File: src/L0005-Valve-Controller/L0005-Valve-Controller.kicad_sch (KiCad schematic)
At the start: 16 parts, among them J1 Jumper_NO, P1 3220-20-0200-00

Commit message: routed rev 2
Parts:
- B1: footprint (none) -> L0005-Valve-Controller:PTS647SM38SMTR2LFS
- C15: value (none) -> 0.1uF; footprint (none) -> L0005-Valve-Controller:CAP_0603
- R26, R27: footprint (none) -> L0005-Valve-Controller:RES_0603
- U1: value (none) -> STM32H750VBTx; footprint (none) -> L0005-Valve-Controller:STM32H750VBT6
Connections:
- net EXECPT: now also U1.60 (PD13); no longer U1.78 (PC10)
- net RX: now also U1.79 (PC11); no longer U1.68 (PA9)
- net TX: now also U1.78 (PC10); no longer U1.69 (PA10)
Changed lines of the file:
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@@
   (junction (at 44.45 68.58) (diameter 0) (color 0 0 0 0)
   )
+  (no_connect (at 104.775 124.46))
+  (no_connect (at 47.625 118.11))
+  (no_connect (at 47.625 115.57))
   (no_connect (at 163.83 87.63))
   (no_connect (at 163.83 95.25))
@@
   (no_connect (at 47.625 86.36))
   (no_connect (at 104.775 167.64))
-  (no_connect (at 104.775 165.1))
   (no_connect (at 104.775 149.86))
   (no_connect (at 104.775 147.32))
@@
   (no_connect (at 47.625 162.56))
   (no_connect (at 47.625 165.1))
-  (no_connect (at 47.625 170.18))
   (no_connect (at 47.625 172.72))
   (no_connect (at 104.775 175.26))
@@
   (no_connect (at 104.775 132.08))
   (no_connect (at 104.775 129.54))
-  (no_connect (at 104.775 124.46))
   (no_connect (at 210.82 76.962))
   (no_connect (at 210.82 61.722))
@@
     (stroke (width 0) (type default) (color 0 0 0 0))
   )
+  (wire (pts (xy 36.83 170.18) (xy 47.625 170.18))
+    (stroke (width 0) (type default) (color 0 0 0 0))
+  )
   (wire (pts (xy 104.775 152.4) (xy 113.03 152.4))
     (stroke (width 0) (type default) (color 0 0 0 0))
@@
     (stroke (width 0) (type default) (color 0 0 0 0))
   )
-  (wire (pts (xy 38.735 118.11) (xy 47.625 118.11))
-    (stroke (width 0) (type default) (color 0 0 0 0))
-  )
   (wire (pts (xy 210.82 64.262) (xy 208.28 64.262))
     (stroke (width 0) (type default) (color 0 0 0 0))
@@
     (stroke (width 0) (type default) (color 0 0 0 0))
   )
+  (wire (pts (xy 104.775 165.1) (xy 113.03 165.1))
+    (stroke (width 0) (type default) (color 0 0 0 0))
+  )
   (polyline (pts (xy 174.625 108.585) (xy 133.985 108.585))
     (stroke (width 0) (type default) (color 0 0 0 0))
@@
     (stroke (width 0) (type default) (color 0 0 0 0))
   )
+  (wire (pts (xy 104.775 162.56) (xy 113.03 162.56))
+    (stroke (width 0) (type default) (color 0 0 0 0))
+  )
   (wire (pts (xy 44.45 55.88) (xy 44.45 53.34))
     (stroke (width 0) (type default) (color 0 0 0 0))
@@
     (stroke (width 0) (type default) (color 0 0 0 0))
   )
-  (wire (pts (xy 104.775 162.56) (xy 113.03 162.56))
-    (stroke (width 0) (type default) (color 0 0 0 0))
-  )
   (wire (pts (xy 208.28 74.422) (xy 208.28 79.502))
     (stroke (width 0) (type default) (color 0 0 0 0))
@@
   )
   (wire (pts (xy 104.775 127) (xy 113.03 127))
-    (stroke (width 0) (type default) (color 0 0 0 0))
-  )
-  (wire (pts (xy 47.625 115.57) (xy 38.735 115.57))
     (stroke (width 0) (type default) (color 0 0 0 0))
   )
@@
     )
   )
-  (global_label "RX" (shape input) (at 38.735 115.57 180) (fields_autoplaced)
-    (effects (font (size 1.27 1.27)) (justify right))
-    (property "Intersheet References" "${INTERSHEET_REFS}" (id 0) (at 5.08 10.795 0)
+  (global_label "RX" (shape input) (at 113.03 165.1 0) (fields_autoplaced)
+    (effects (font (size 1.27 1.27)) (justify left))
+    (property "Intersheet References" "${INTERSHEET_REFS}" (id 0) (at 146.685 269.875 0)
       (effects (font (size 1.27 1.27)) hide)
     )
@@
     )
   )
-  (global_label "EXECPT" (shape input) (at 113.03 162.56 0) (fields_autoplaced)
-    (effects (font (size 1.27 1.27)) (justify left))
-    (property "Intersheet References" "${INTERSHEET_REFS}" (id 0) (at -5.08 196.215 0)
-      (effects (font (size 1.27 1.27)) (justify left) hide)
+  (global_label "EXECPT" (shape input) (at 36.83 170.18 180) (fields_autoplaced)
+    (effects (font (size 1.27 1.27)) (justify right))
+    (property "Intersheet References" "${INTERSHEET_REFS}" (id 0) (at 154.94 136.525 0)
+      (effects (font (size 1.27 1.27)) (justify right) hide)
     )
   )
@@
     )
   )
-  (global_label "TX" (shape input) (at 38.735 118.11 180) (fields_autoplaced)
-    (effects (font (size 1.27 1.27)) (justify right))
-    (property "Intersheet References" "${INTERSHEET_REFS}" (id 0) (at 5.08 10.795 0)
+  (global_label "TX" (shape input) (at 113.03 162.56 0) (fields_autoplaced)
+    (effects (font (size 1.27 1.27)) (justify left))
+    (property "Intersheet References" "${INTERSHEET_REFS}" (id 0) (at 146.685 269.875 0)
       (effects (font (size 1.27 1.27)) hide)
     )
@@
       (effects (font (size 1.27 1.27)) hide)
     )
-    (property "Value" "" (id 1) (at 24.765 77.851 0)
+    (property "Value" "Earth" (id 1) (at 24.765 77.851 0)
       (effects (font (size 1.27 1.27)) hide)
     )
@@
       (effects (font (size 1.524 1.524)) hide)
     )
-    (property "Footprint" "" (id 2) (at 157.48 102.87 0)
+    (property "Footprint" "L0005-Valve-Controller:PTS647SM38SMTR2LFS" (id 2) (at 157.48 102.87 0)
       (effects (font (size 1.524 1.524)) hide)
     )
@@
       (effects (font (size 1.27 1.27)) (justify right))
     )
-    (property "Footprint" "" (id 2) (at 204.597 42.672 0)
+    (property "Footprint" "L0005-Valve-Controller:RES_0603" (id 2) (at 204.597 42.672 0)
       (effects (font (size 1.27 1.27)) (justify left bottom) hide)
     )
@@
       (effects (font (size 1.27 1.27)) (justify right))
     )
-    (property "Value" "" (id 1) (at 140.97 93.345 90)
+    (property "Value" "0.1uF" (id 1) (at 140.97 93.345 90)
       (effects (font (size 1.27 1.27)) (justify right))
     )
-    (property "Footprint" "" (id 2) (at 158.75 93.98 0)
+    (property "Footprint" "L0005-Valve-Controller:CAP_0603" (id 2) (at 158.75 93.98 0)
       (effects (font (size 1.27 1.27)) (justify left bottom) hide)
     )
@@
       (effects (font (size 1.27 1.27)) (justify right))
     )
-    (property "Footprint" "" (id 2) (at 215.265 42.672 0)
+    (property "Footprint" "L0005-Valve-Controller:RES_0603" (id 2) (at 215.265 42.672 0)
       (effects (font (size 1.27 1.27)) (justify left bottom) hide)
     )
@@
     (in_bom yes) (on_board yes)
     (property "Reference" "U1" (id 0) (at 76.2 36.195 0))
-    (property "Value" "" (id 1) (at 76.2 36.9371 0)
-      (effects (font (size 1.27 1.27)) hide)
-    )
-    (property "Footprint" "" (id 2) (at 52.705 177.8 0)
+    (property "Value" "STM32H750VBTx" (id 1) (at 76.2 36.9371 0)
+      (effects (font (size 1.27 1.27)) hide)
+    )
+    (property "Footprint" "L0005-Valve-Controller:STM32H750VBT6" (id 2) (at 52.705 177.8 0)
       (effects (font (size 1.27 1.27)) (justify right) hide)
     )
@@
       (reference "#PWR035") (unit 1) (value "Earth") (footprint "")
     )
+    (path "/a9eaeea5-207e-44f5-b9ad-eca9290d0207/8f9521e7-a6d2-4346-87ca-d9528ce59a50"
+      (reference "#PWR?") (unit 1) (value "Earth") (footprint "")
+    )
     (path "/00000000-0000-0000-0000-000062045c3c"

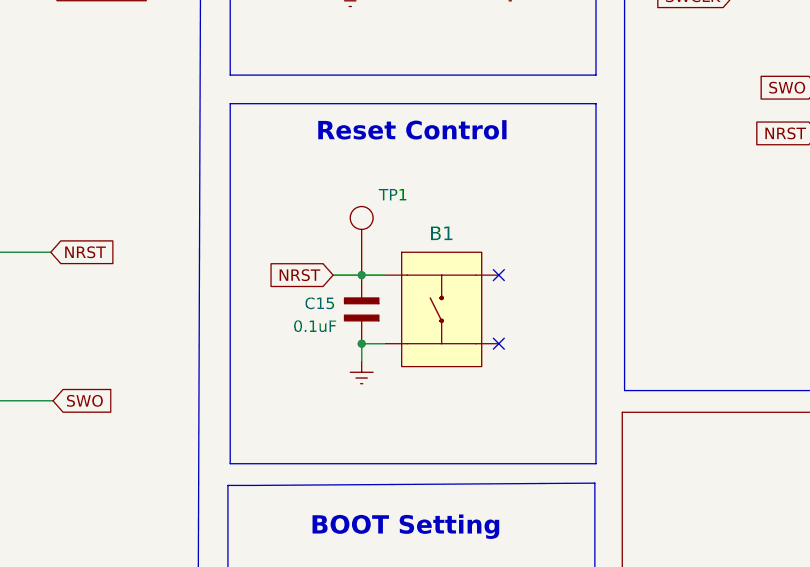
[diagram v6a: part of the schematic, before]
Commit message: added NO jumper to MCU reset button
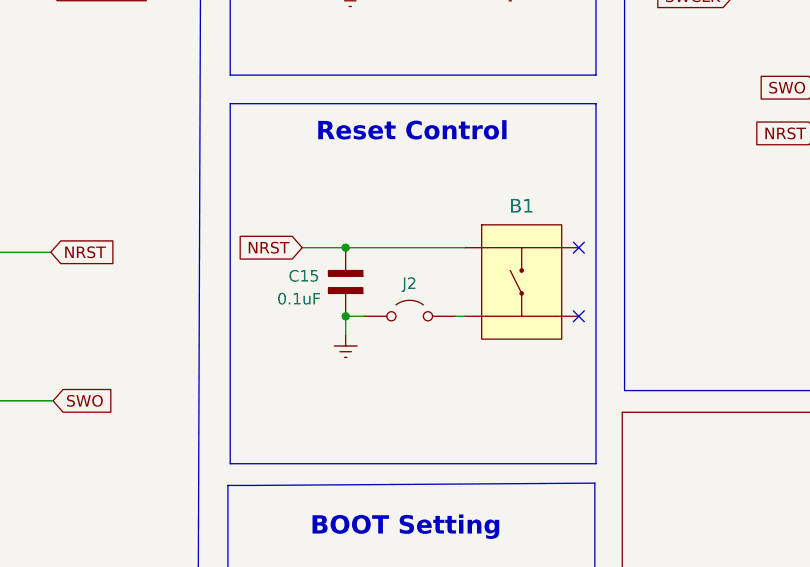
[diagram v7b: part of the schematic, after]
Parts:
- removed TP1: TP, L0005-Valve-Controller:TP, symbol L0005-Valve-Controller:TP
- added J2: Jumper_NO, L0005-Valve-Controller:Jumper-NO, symbol L0005-Valve-Controller:Jumper_NO
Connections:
- net Earth: now also J2.1 (A); no longer B1.3
- new net: B1.3, J2.2 (B)
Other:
- moved on the sheet: B1, C15

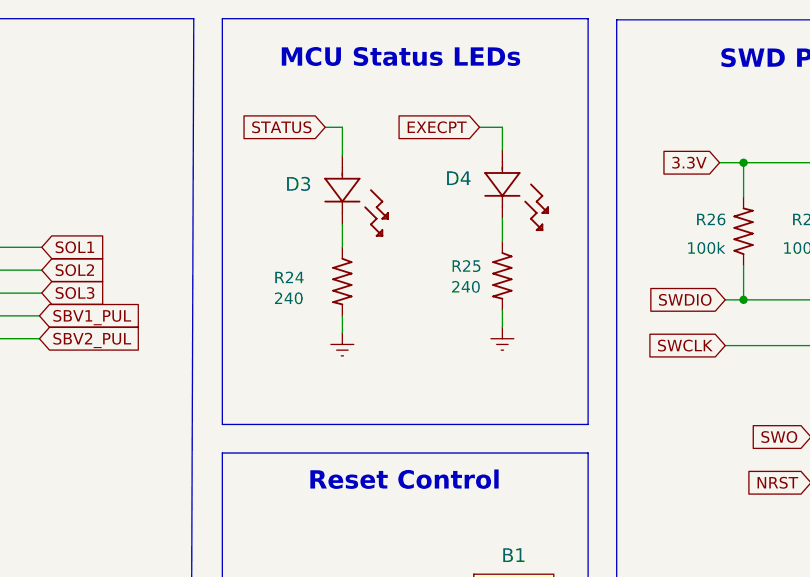
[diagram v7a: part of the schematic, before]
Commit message: changed level shifter to opendrain mosfet for pulse interface
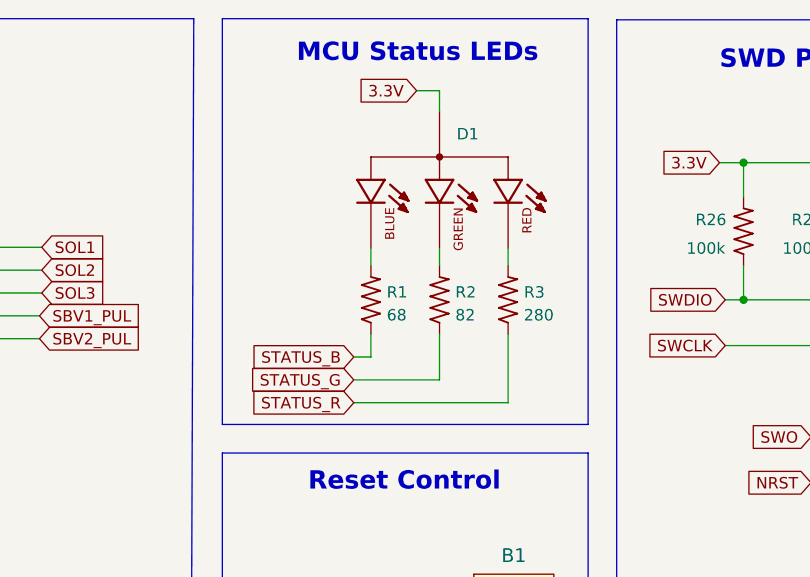
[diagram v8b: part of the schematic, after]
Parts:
- removed D3: LED_AMBER, L0005-Valve-Controller:150120AS75000, symbol L0005-Valve-Controller:LED_AMBER
- removed D4: LED_RED, L0005-Valve-Controller:LED_RED, symbol L0005-Valve-Controller:LED_RED
- removed R24, R25: 240, L0005-Valve-Controller:RES_0603, symbol L0005-Valve-Controller:RES_0603
- added D1: CLMVC-FKA-CL1D1L71BB7C3C3, LED_CLMVC-FKA-CL1D1L71BB7C3C3, symbol Flight-Computer:CLMVC-FKA-CL1D1L71BB7C3C3
- added R1: 68, Flight-Computer:RES_0603, symbol Flight-Computer:RES_0603
- added R2: 82, Flight-Computer:RES_0603, symbol Flight-Computer:RES_0603
- added R3: 280, Flight-Computer:RES_0603, symbol Flight-Computer:RES_0603
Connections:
- net 3.3V: now also D1.1
- new net: D1.4, R3.2
- new net: D1.2, R1.2
- new net: D1.3, R2.2
- new net STATUS_B: R1.1
- new net STATUS_G: R2.1
- new net STATUS_R: R3.1
